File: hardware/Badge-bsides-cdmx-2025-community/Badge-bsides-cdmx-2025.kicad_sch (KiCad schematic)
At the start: 43 parts, among them J1 SWDIO, J3 ADDON, J4 Conn_01x04_Pin, J5 I2C, J6 Conn_01x04_Pin, P6 USB_C_Plug_USB2.0, Q3 DMG3415U-7, SW10 SW_Push, SW11 ON, SW2 RESET, SW7 SW_Push, SW8 SW_Push, SW9 SW_Push, U1 PY32F030F28U6TR, U6 AP2112K-3.3

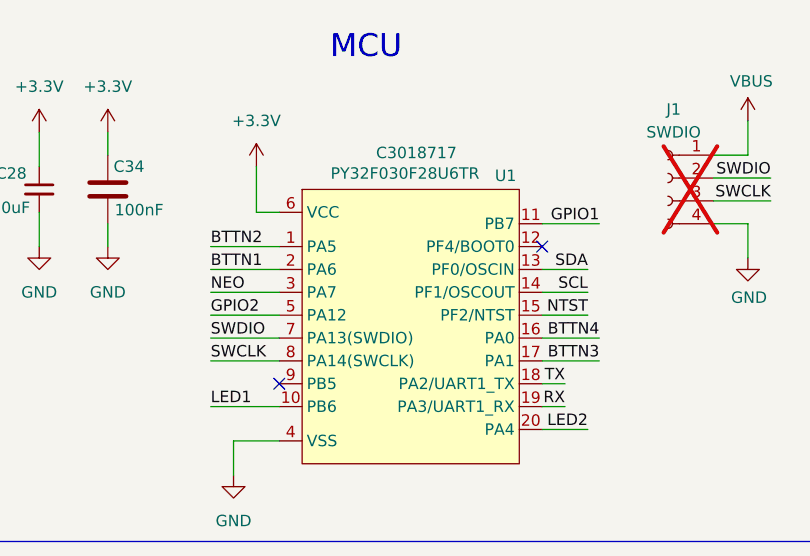
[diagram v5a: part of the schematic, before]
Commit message: feat(Hw):BoM_Updated_Staff_Community
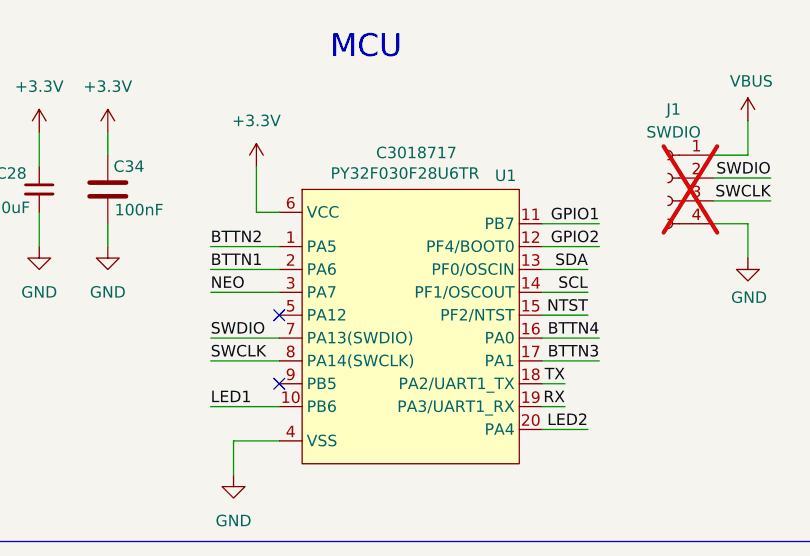
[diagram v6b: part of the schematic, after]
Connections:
- net GPIO2: now also U1.12 (PF4/BOOT0); no longer U1.5 (PA12)
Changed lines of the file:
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@@
 	)
 	(no_connect
-		(at 251.46 36.83)
+		(at 222.25 44.45)
 	)
 	(no_connect
@@
 	(wire
 		(pts
-			(xy 214.63 44.45) (xy 222.25 44.45)
-		)
-		(stroke
-			(width 0)
-			(type default)
-		)
-	)
-	(wire
-		(pts
 			(xy 251.46 52.07) (xy 254 52.07)
 		)
@@
 		(pts
 			(xy 66.548 38.1) (xy 69.088 38.1)
+		)
+		(stroke
+			(width 0)
+			(type default)
+		)
+	)
+	(wire
+		(pts
+			(xy 257.81 36.83) (xy 251.46 36.83)
 		)
 		(stroke
@@
 	)
 	(label "GPIO2"
-		(at 214.63 44.45 0)
+		(at 257.81 36.83 180)
 		(effects
 			(font
 				(size 1.27 1.27)
 			)
-			(justify left bottom)
-		)
-	)
+			(justify right bottom)
+		)
+	)

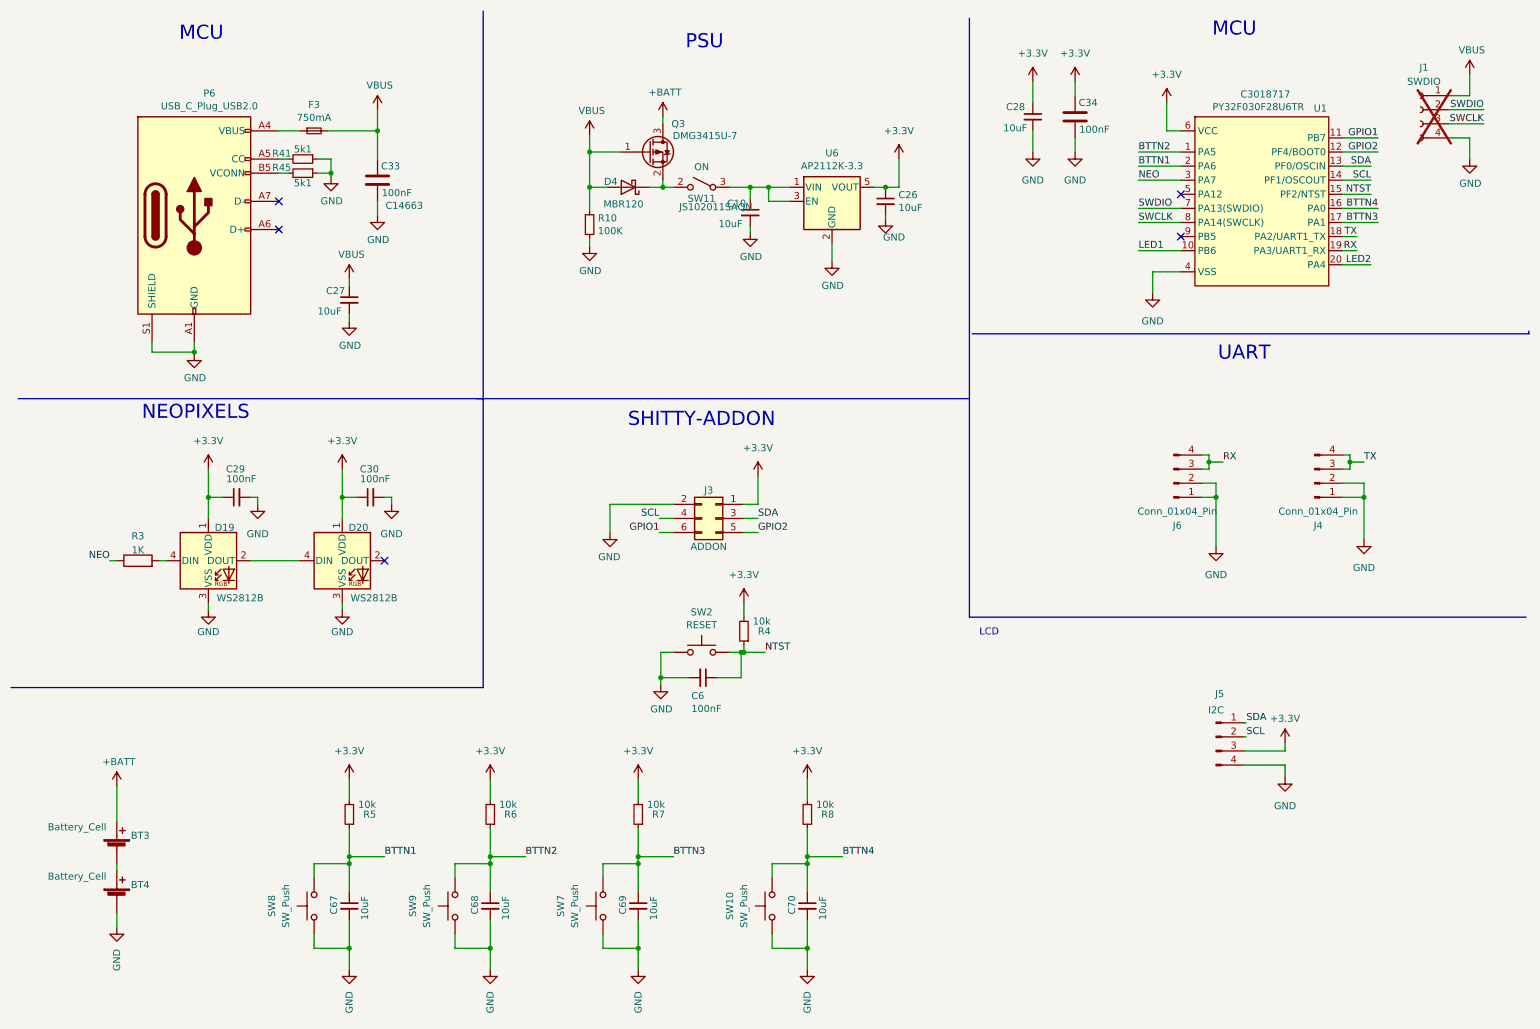
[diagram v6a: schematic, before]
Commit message: feat(Hw)USB_C_Deleted
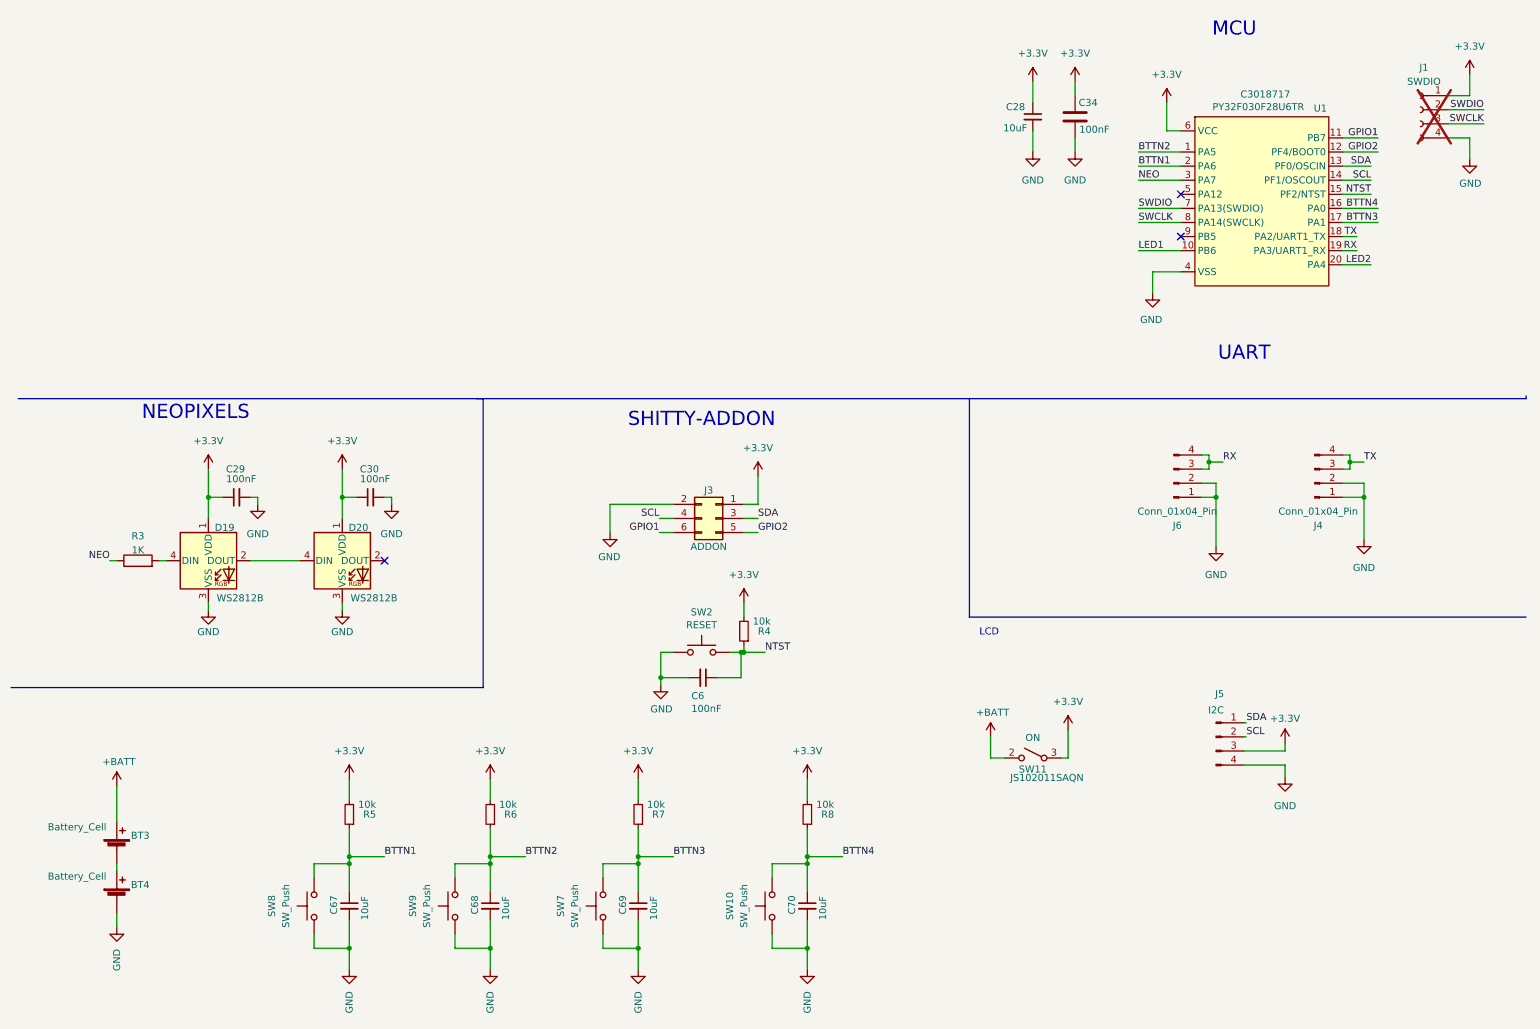
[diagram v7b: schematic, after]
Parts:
- removed C10, C26, C27: 10uF, Capacitor_SMD:C_0603_1608Metric, symbol Device:C_Small
- removed C33: 100nF, Capacitor_SMD:C_0603_1608Metric, symbol Device:C
- removed D4: MBR120, Diode_SMD:D_SOD-123F, symbol Diode:MBR340
- removed F3: 750mA, Fuse:Fuse_0603_1608Metric, symbol Device:Fuse_Small
- removed P6: USB_C_Plug_USB2.0, Footprints:C393939, symbol HunterCat-NFC-rescue:USB_C_Plug_USB2.0-Connector
- removed Q3: DMG3415U-7, Package_TO_SOT_SMD:SOT-23, symbol Device:Q_PMOS_GSD
- removed R10: 100K, Resistor_SMD:R_0603_1608Metric, symbol Device:R_Small
- removed R41, R45: 5k1, Resistor_SMD:R_0603_1608Metric, symbol Device:R_Small
- removed U6: AP2112K-3.3, Package_TO_SOT_SMD:SOT-23-5, symbol HunterCat-NFC-rescue:AP2112K-3.3-Regulator_Linear
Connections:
- net VBUS is gone; now on net +3.3V: J1.1 (Pin_1)
- net +3.3V: now also SW11.3 (A)
- net +BATT: now also SW11.2 (B)
- no-connect marks 5 -> 3
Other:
- note removed: "PSU"
- moved on the sheet: SW11

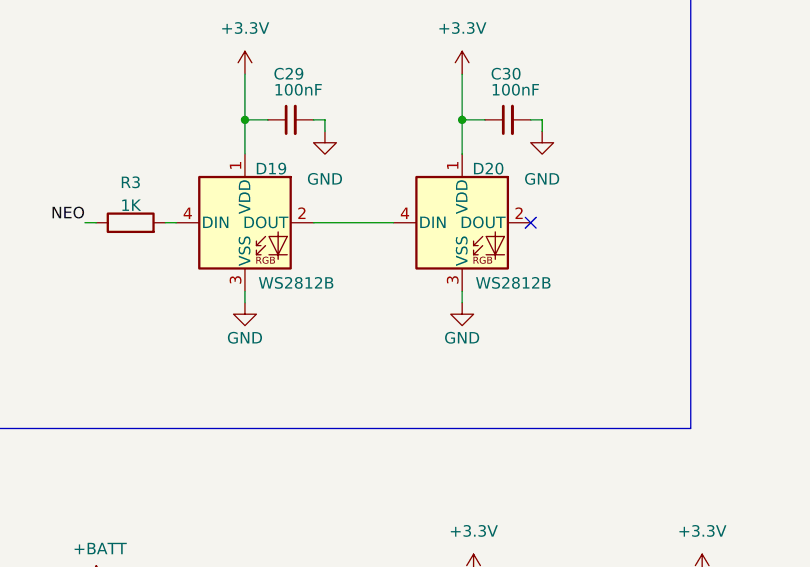
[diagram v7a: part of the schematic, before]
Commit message: Fix(Hw): Fixed_BOM(Staff,Community, Speaker)
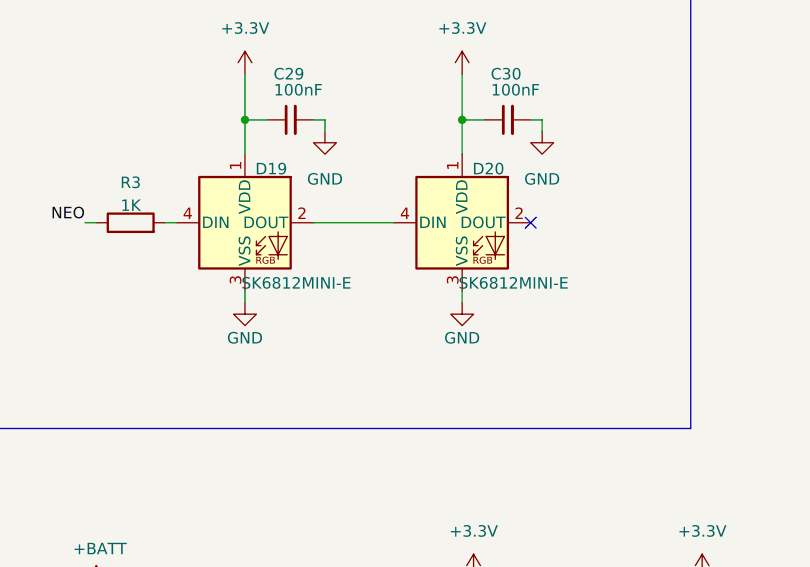
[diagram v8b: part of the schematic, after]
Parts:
- C29, C30: LCSC# C478888 -> C66501
- C34, C6: LCSC# C14663 -> C66501
- D19, D20: value WS2812B -> SK6812MINI-E; LCSC# C527089 -> C5149201; manf# WS2812B-Mini -> (none)
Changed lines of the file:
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@@
 			)
 		)
-		(property "Value" "WS2812B"
+		(property "Value" "SK6812MINI-E"
 			(at 76.835 117.221 0)
 			(effects
@@
 			)
 		)
-		(property "LCSC#" "C527089"
+		(property "LCSC#" "C5149201"
 			(at 71.12 110.49 0)
 			(effects
@@
 			)
 		)
-		(property "manf#" "WS2812B-Mini"
+		(property "manf#" ""
 			(at 71.12 110.49 0)
 			(effects
@@
 			)
 		)
-		(property "LCSC#" "C478888"
+		(property "LCSC#" "C66501"
 			(at 76.2 99.06 0)
 			(effects
@@
 			)
 		)
-		(property "LCSC#" "C478888"
+		(property "LCSC#" "C66501"
 			(at 52.07 99.06 0)
 			(effects
@@
 			)
 		)
-		(property "LCSC#" "C14663"
+		(property "LCSC#" "C66501"
 			(at 136.144 131.572 0)
 			(effects
@@
 			)
 		)
-		(property "LCSC#" "C14663"
+		(property "LCSC#" "C66501"
 			(at 209.296 30.48 0)
 			(effects
@@
 			)
 		)
-		(property "Value" "WS2812B"
+		(property "Value" "SK6812MINI-E"
 			(at 52.705 117.221 0)
 			(effects
@@
 			)
 		)
-		(property "LCSC#" "C527089"
+		(property "LCSC#" "C5149201"
 			(at 46.99 110.49 0)
 			(effects
@@
 			)
 		)
-		(property "manf#" "WS2812B-Mini"
+		(property "manf#" ""
 			(at 46.99 110.49 0)
 			(effects
